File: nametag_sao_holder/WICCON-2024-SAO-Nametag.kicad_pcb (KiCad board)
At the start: 2 copper layers, 150 x 137.2 mm, 25 parts, among them J1 SAO, J2 SAO, J3 SAO, J4 SAO, J5 SAO, J6 SAO, J7 SAO, J8 SAO, SW1 ON/OFF, U1 QX2303L33E

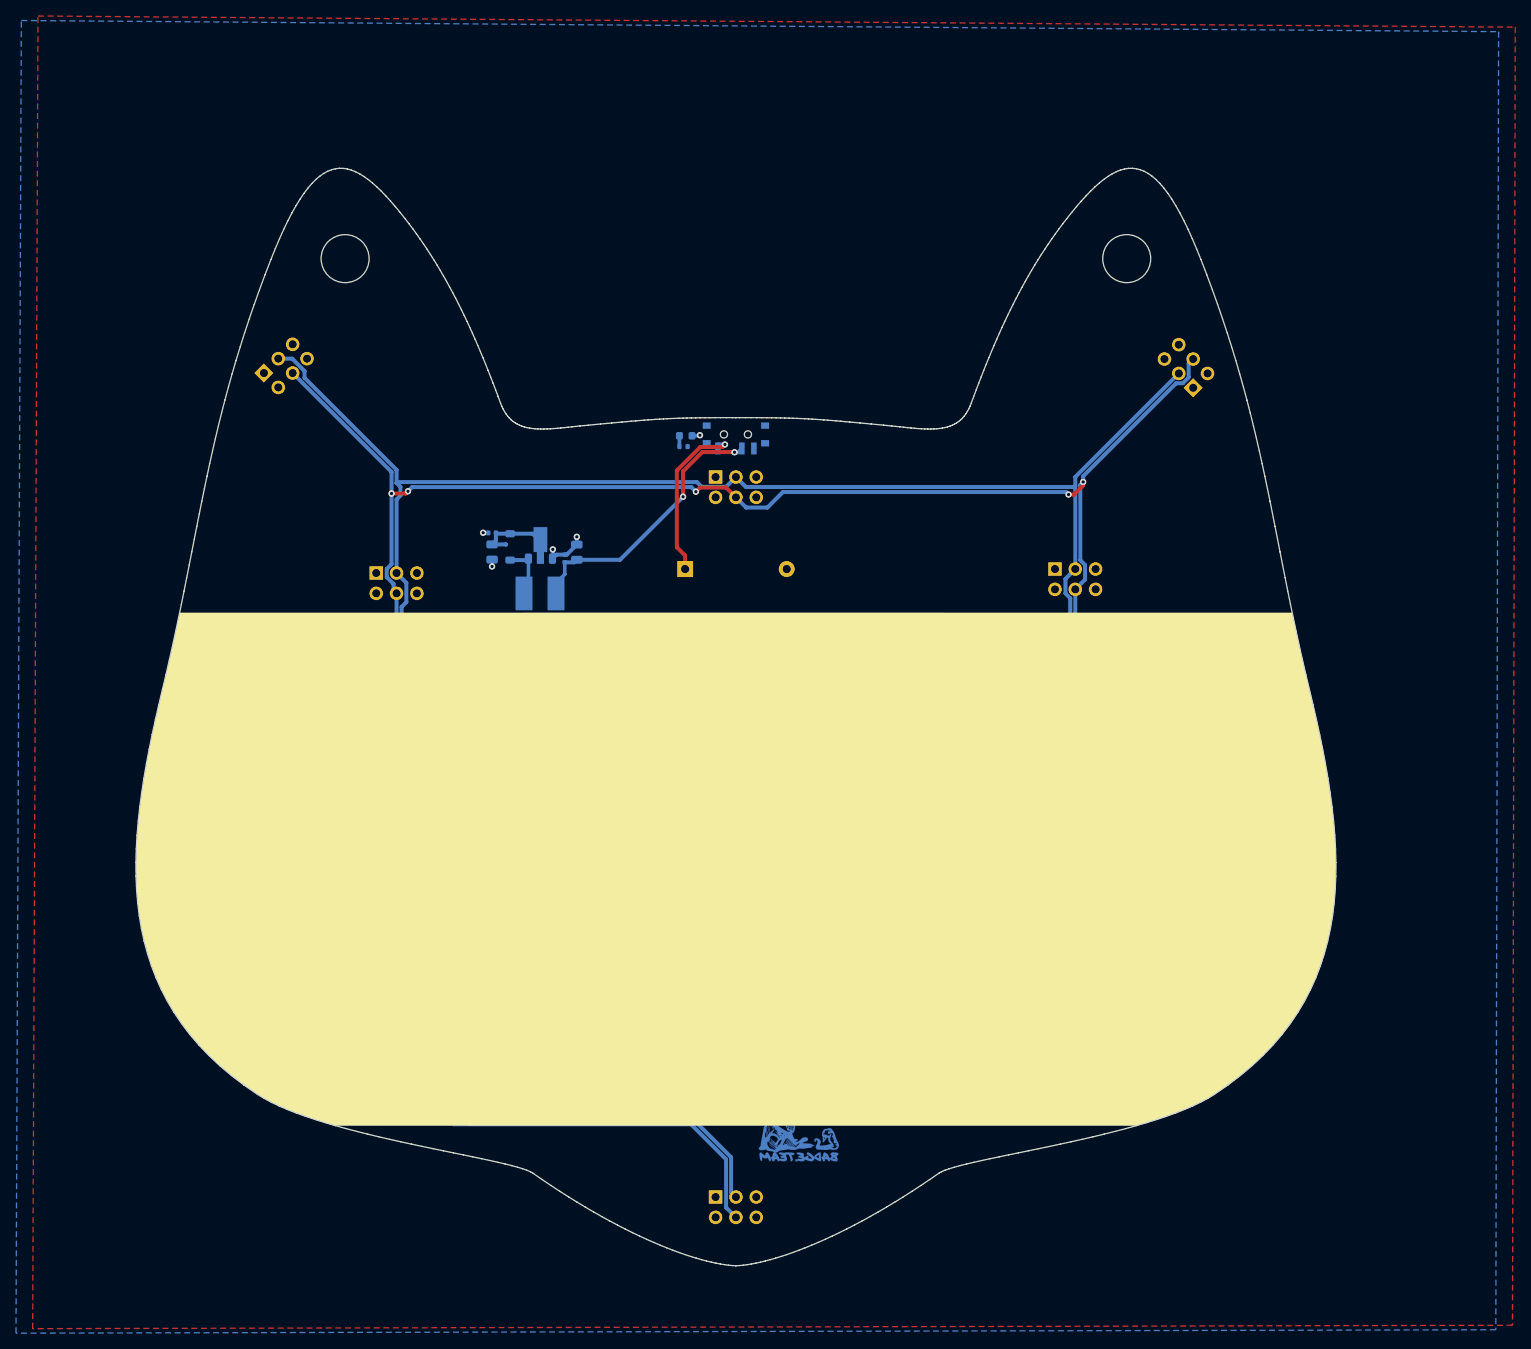
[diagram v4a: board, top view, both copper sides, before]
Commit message: Fix I2C troubles, add connectors
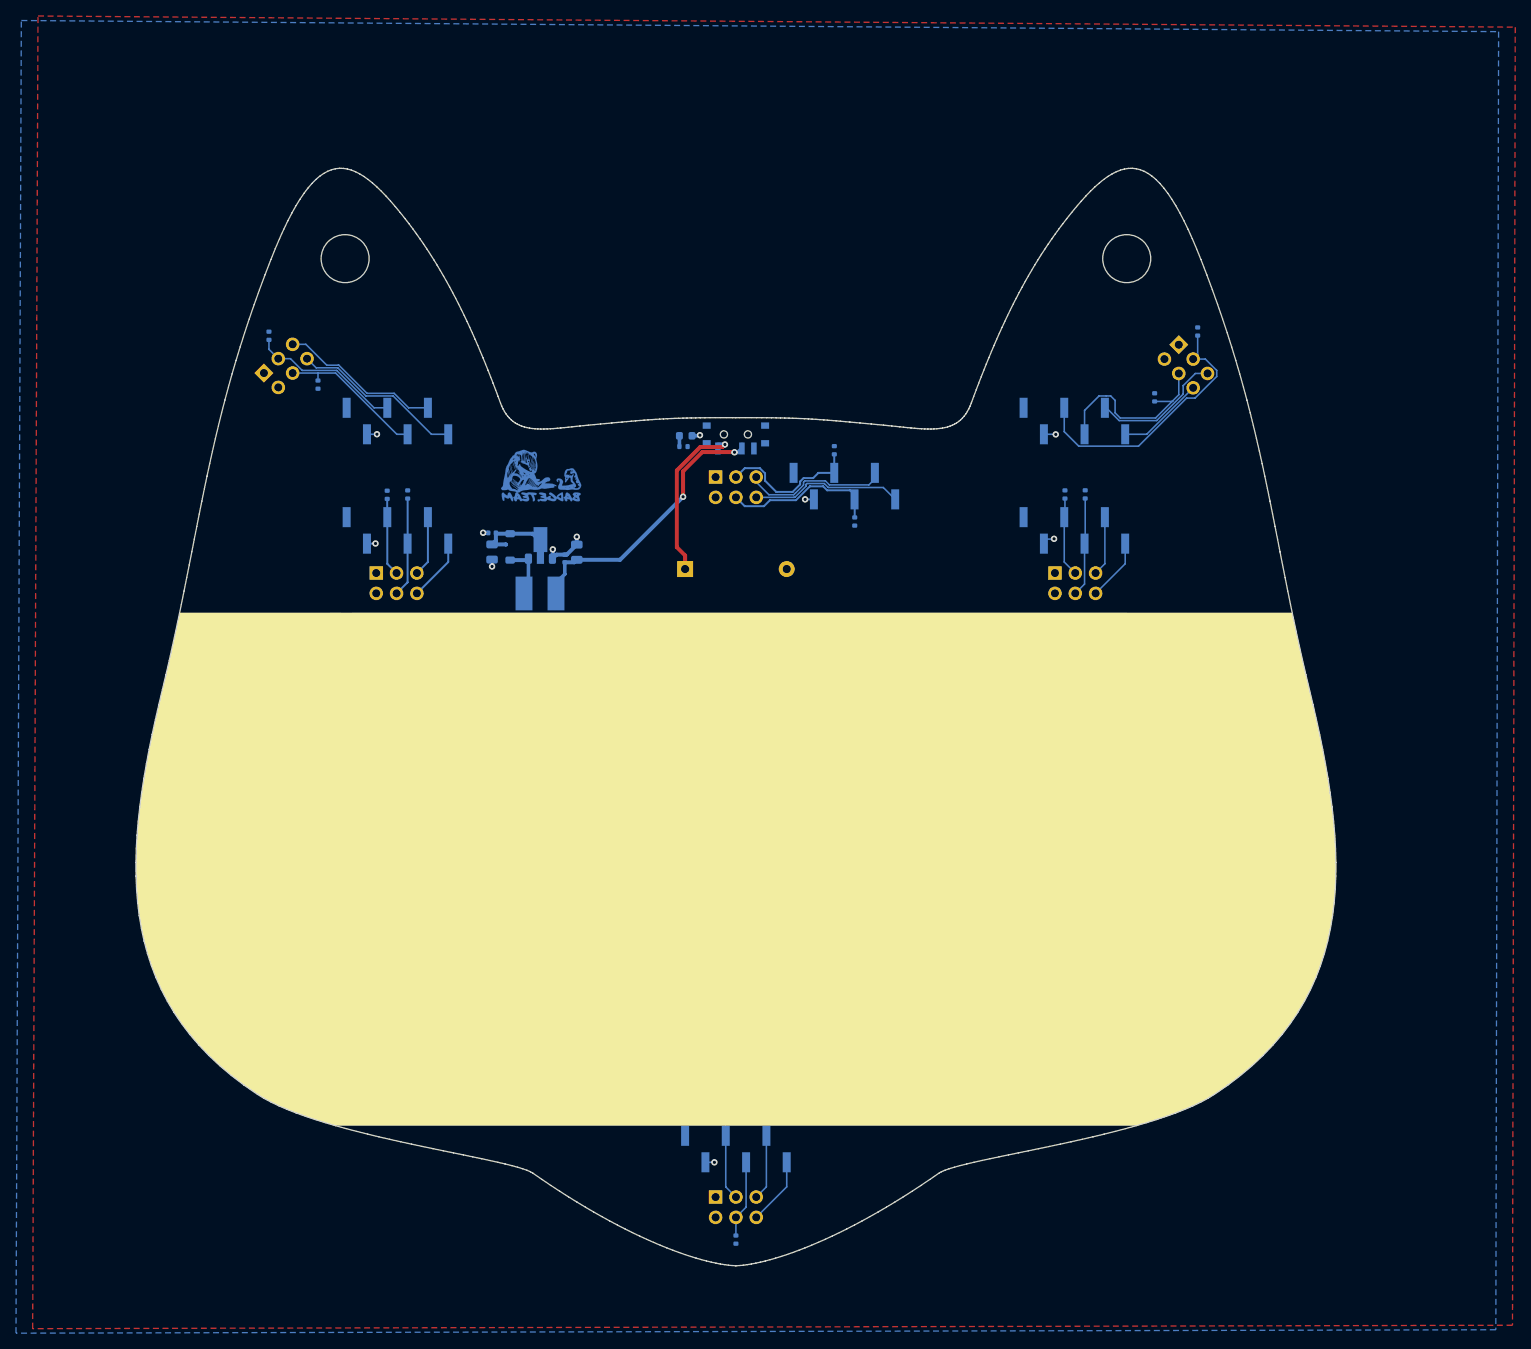
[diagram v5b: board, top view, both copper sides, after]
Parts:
- added J10: MOD2, Connector_PinHeader_2.54mm:PinHeader_1x06_P2.54mm_Vertical_SMD_Pin1Left, B.Cu at (-42.3, -23.3)
- added J11: MOD3, Connector_PinHeader_2.54mm:PinHeader_1x06_P2.54mm_Vertical_SMD_Pin1Left, B.Cu at (-42.4, 39.7)
- added J12: MOD4, Connector_PinHeader_2.54mm:PinHeader_1x06_P2.54mm_Vertical_SMD_Pin1Left, B.Cu at (42.3, -23.3)
- added J13: MOD5, Connector_PinHeader_2.54mm:PinHeader_1x06_P2.54mm_Vertical_SMD_Pin1Left, B.Cu at (42.2, 39.7)
- added J14: MOD6, Connector_PinHeader_2.54mm:PinHeader_1x06_P2.54mm_Vertical_SMD_Pin1Left, B.Cu at (-42.3, -37.0)
- added J15: MOD7, Connector_PinHeader_2.54mm:PinHeader_1x06_P2.54mm_Vertical_SMD_Pin1Left, B.Cu at (0.00, 54.0)
- added J16: MOD8, Connector_PinHeader_2.54mm:PinHeader_1x06_P2.54mm_Vertical_SMD_Pin1Left, B.Cu at (42.3, -37.0)
- added J9: MOD1, Connector_PinHeader_2.54mm:PinHeader_1x06_P2.54mm_Vertical_SMD_Pin1Left, B.Cu at (13.6, -28.9)
- added R10: 4.7k, Resistor_SMD:R_0402_1005Metric, B.Cu at (54.9, 33.3)
- added R11: 4.7k, Resistor_SMD:R_0402_1005Metric, B.Cu at (54.9, 41.3)
- added R12: 4.7k, Resistor_SMD:R_0402_1005Metric, B.Cu at (-58.4, -47.7)
- added R13: 4.7k, Resistor_SMD:R_0402_1005Metric, B.Cu at (-52.2, -41.5)
- added R14: 4.7k, Resistor_SMD:R_0402_1005Metric, B.Cu at (-1.28, 49.5)
- added R15: 4.7k, Resistor_SMD:R_0402_1005Metric, B.Cu at (0.00, 65.3)
- added R16: 4.7k, Resistor_SMD:R_0402_1005Metric, B.Cu at (57.7, -48.2)
- added R17: 4.7k, Resistor_SMD:R_0402_1005Metric, B.Cu at (52.3, -40.0)
- added R2: 4.7k, Resistor_SMD:R_0402_1005Metric, B.Cu at (12.3, -33.4)
- added R3: 4.7k, Resistor_SMD:R_0402_1005Metric, B.Cu at (14.8, -24.4)
- added R4: 4.7k, Resistor_SMD:R_0402_1005Metric, B.Cu at (-43.6, -27.8)
- added R5: 4.7k, Resistor_SMD:R_0402_1005Metric, B.Cu at (-41.0, -27.8)
- added R6: 4.7k, Resistor_SMD:R_0402_1005Metric, B.Cu at (-55.5, 33.8)
- added R7: 4.7k, Resistor_SMD:R_0402_1005Metric, B.Cu at (-54.9, 41.3)
- added R8: 4.7k, Resistor_SMD:R_0402_1005Metric, B.Cu at (41.1, -27.8)
- added R9: 4.7k, Resistor_SMD:R_0402_1005Metric, B.Cu at (43.7, -27.8)
- moved N2 88.6 mm to (-24.3, -30.2)
- moved J8 5.68 mm to (55.4, -46.5), turned to 45 degrees
- moved J4 0.50 mm to (39.9, -18.0)
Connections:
- J1 pad 3: SDA -> SDA1
- J1 pad 4: SCL -> SCL1
- J1 pad 5: unconnected-(J1-Pin_5-Pad5) -> IO1_1
- J1 pad 6: unconnected-(J1-Pin_6-Pad6) -> IO2_1
- J2 pad 3: SDA -> SDA2
- J2 pad 4: SCL -> SCL2
- J2 pad 5: unconnected-(J2-Pin_5-Pad5) -> IO1_2
- J2 pad 6: unconnected-(J2-Pin_6-Pad6) -> IO2_2
- J3 pad 3: SDA -> SDA3
- J3 pad 4: SCL -> SCL3
- J3 pad 5: unconnected-(J3-Pin_5-Pad5) -> IO1_3
- J3 pad 6: unconnected-(J3-Pin_6-Pad6) -> IO2_3
- J4 pad 3: SDA -> SDA4
- J4 pad 4: SCL -> SCL4
- J4 pad 5: unconnected-(J4-Pin_5-Pad5) -> IO1_4
- J4 pad 6: unconnected-(J4-Pin_6-Pad6) -> IO2_4
- J5 pad 3: SDA -> SDA5
- J5 pad 4: SCL -> SCL5
- J5 pad 5: unconnected-(J5-Pin_5-Pad5) -> IO1_5
- J5 pad 6: unconnected-(J5-Pin_6-Pad6) -> IO2_5
- J6 pad 3: SDA -> SDA6
- J6 pad 4: SCL -> SCL6
- J6 pad 5: unconnected-(J6-Pin_5-Pad5) -> IO1_6
- J6 pad 6: unconnected-(J6-Pin_6-Pad6) -> IO2_6
- J7 pad 3: SDA -> SDA7
- J7 pad 4: SCL -> SCL7
- J7 pad 5: unconnected-(J7-Pin_5-Pad5) -> IO1_7
- J7 pad 6: unconnected-(J7-Pin_6-Pad6) -> IO2_7
- J8 pad 3: SDA -> SDA8
- J8 pad 4: SCL -> SCL8
- J8 pad 5: unconnected-(J8-Pin_5-Pad5) -> IO1_8
- J8 pad 6: unconnected-(J8-Pin_6-Pad6) -> IO2_8
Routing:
- net SCL: track 347.1 -> 0.00 mm, vias 5 -> 0
- net SDA: track 338.8 -> 0.00 mm, vias 1 -> 0
- net SDA8: track 0.00 -> 33.9 mm
- net SCL8: track 0.00 -> 23.7 mm
- net IO2_6: track 0.00 -> 21.6 mm
- net SCL1: track 0.00 -> 20.4 mm
- net IO1_6: track 0.00 -> 20.2 mm
- net SCL3: track 0.00 -> 19.2 mm
- net SDA3: track 0.00 -> 19.1 mm
- net IO2_1: track 0.00 -> 19.0 mm
- net SDA6: track 0.00 -> 19.0 mm
- net SCL6: track 0.00 -> 18.5 mm
- net IO2_3: track 0.00 -> 18.4 mm
- net IO1_1: track 0.00 -> 18.3 mm
- net IO1_3: track 0.00 -> 18.2 mm
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
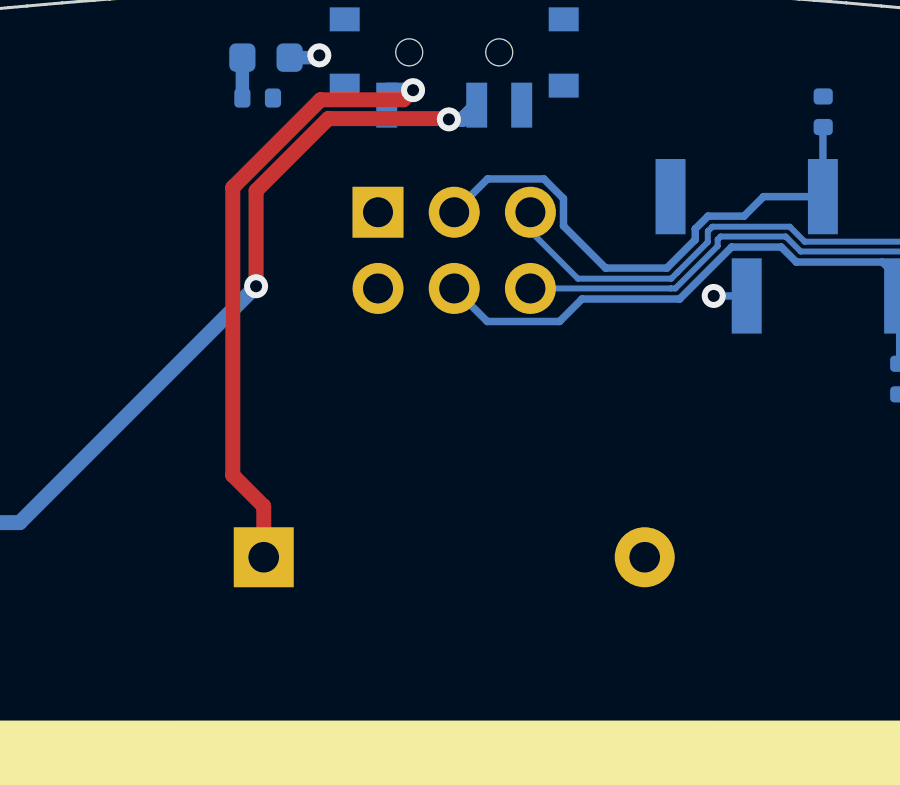
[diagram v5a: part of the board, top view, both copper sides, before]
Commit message: Add 100k pull-up to SDA on social battery and use correct footprint for battery holder on SAO nametag
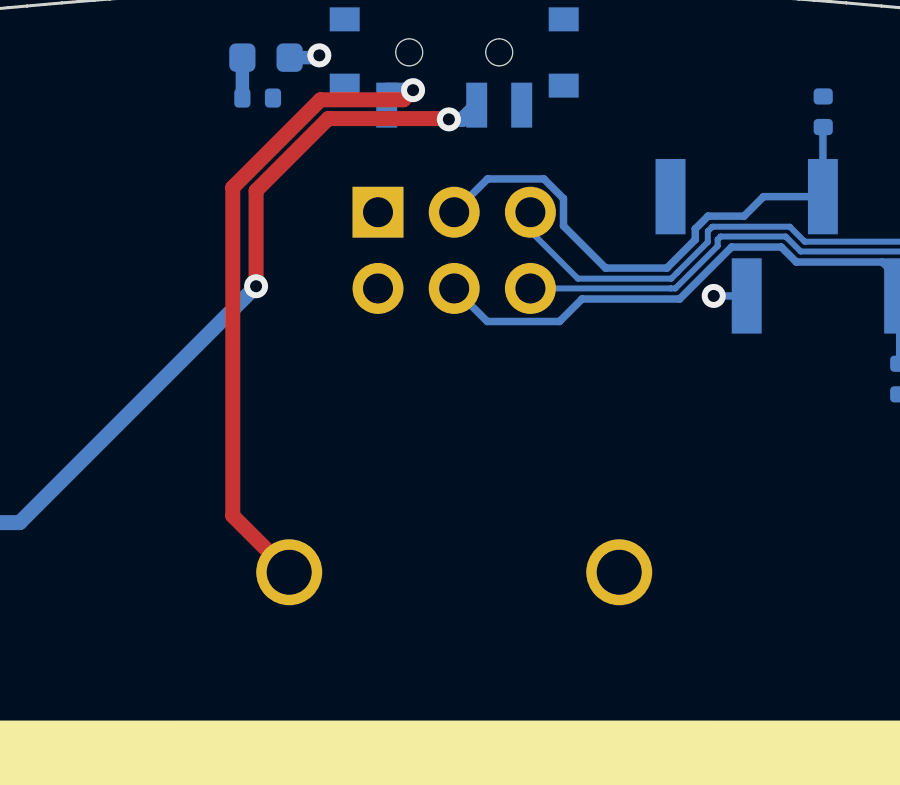
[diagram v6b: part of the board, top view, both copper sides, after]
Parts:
- BT1: footprint Library:BatteryHolder_Keystone_2468_2xAAA_noholes -> Library:BAT-TH_BH-BH-AAA-A1AJ020
- moved BT1 6.37 mm to (0.00, -18.0), turned to 90 degrees
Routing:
- net Net-(BT1-+): track 21.0 -> 21.8 mm
